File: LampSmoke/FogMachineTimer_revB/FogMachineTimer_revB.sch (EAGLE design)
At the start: 5 parts, among them IC1 ATTINY85-20SU, J1 M20-9980346, J2 CUI_PJ-037ACUI_PJ-037A_0_0, U1 LH1540AABTR

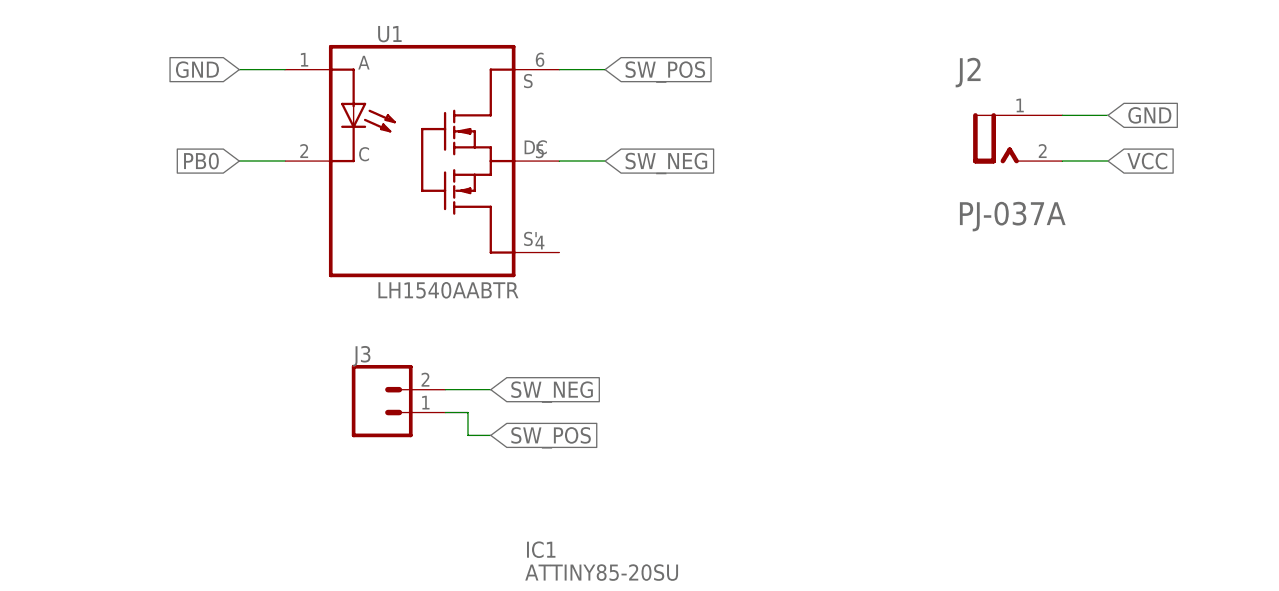
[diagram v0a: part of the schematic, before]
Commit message: corrected polarity
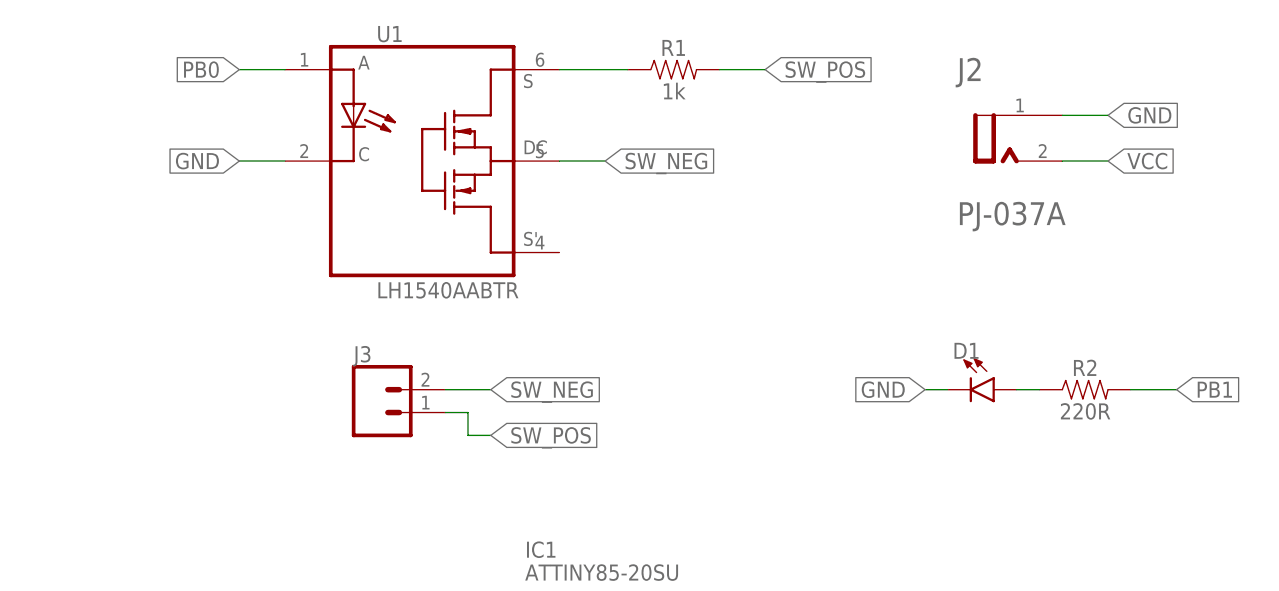
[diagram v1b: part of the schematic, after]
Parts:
- added D1: (no value), SparkFun-LED:LED1206
- added R1: 1k, SparkFun-Resistors:1KOHM-0603-1/10W-1%
- added R2: 220R, SparkFun-Resistors:1KOHM-0603-1/10W-1%
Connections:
- new net N$1: D1.A, R2.1
- new net U1_P6: R1.1, U1.S
- net GND: now also D1.C, U1.C; no longer U1.A
- net PB0: now also U1.A; no longer U1.C
- net PB1: now also R2.2
- net SW_POS: now also R1.2; no longer U1.S
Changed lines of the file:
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@@
 <part name="J2" library="NickParts" library_urn="urn:adsk.eagle:library:4753178" deviceset="CUI_PJ-037A" device="CUI_PJ-037A_0_0" package3d_urn="urn:adsk.eagle:package:4865637/3"/>
 <part name="J3" library="SparkFun-Connectors" library_urn="urn:adsk.eagle:library:513" deviceset="CONN_02" device="" package3d_urn="urn:adsk.eagle:package:38039/1"/>
+<part name="R1" library="SparkFun-Resistors" library_urn="urn:adsk.eagle:library:532" deviceset="1KOHM" device="-0603-1/10W-1%" package3d_urn="urn:adsk.eagle:package:39650/1" value="1k"/>
+<part name="D1" library="SparkFun-LED" library_urn="urn:adsk.eagle:library:529" deviceset="LED" device="1206" package3d_urn="urn:adsk.eagle:package:39352/1"/>
+<part name="R2" library="SparkFun-Resistors" library_urn="urn:adsk.eagle:library:532" deviceset="1KOHM" device="-0603-1/10W-1%" package3d_urn="urn:adsk.eagle:package:39650/1" value="220R"/>
 </parts>
 <sheets>
@@
 <attribute name="NAME" x="30.48" y="102.108" size="1.778" layer="95" font="vector"/>
 </instance>
+<instance part="R1" gate="G$1" x="66.04" y="134.62" smashed="yes">
+<attribute name="NAME" x="66.04" y="136.144" size="1.778" layer="95" font="vector" align="bottom-center"/>
+<attribute name="VALUE" x="66.04" y="133.096" size="1.778" layer="96" font="vector" align="top-center"/>
+</instance>
+<instance part="D1" gate="G$1" x="101.6" y="99.06" smashed="yes" rot="R270">
+<attribute name="NAME" x="97.028" y="102.489" size="1.778" layer="95" font="vector"/>
+<attribute name="VALUE" x="97.028" y="97.155" size="1.778" layer="96" font="vector" align="top-left"/>
+</instance>
+<instance part="R2" gate="G$1" x="111.76" y="99.06" smashed="yes">
+<attribute name="NAME" x="111.76" y="100.584" size="1.778" layer="95" font="vector" align="bottom-center"/>
+<attribute name="VALUE" x="111.76" y="97.536" size="1.778" layer="96" font="vector" align="top-center"/>
+</instance>
 </instances>
 <busses>
@@
 </segment>
 <segment>
+<pinref part="J2" gate="G$0" pin="1"/>
+<wire x1="109.22" y1="129.54" x2="114.3" y2="129.54" width="0.1524" layer="91"/>
+<label x="114.3" y="129.54" size="1.778" layer="95" xref="yes"/>
+</segment>
+<segment>
+<pinref part="U1" gate="G$1" pin="C"/>
+<wire x1="22.86" y1="124.46" x2="17.78" y2="124.46" width="0.1524" layer="91"/>
+<label x="17.78" y="124.46" size="1.778" layer="95" rot="R180" xref="yes"/>
+</segment>
+<segment>
+<pinref part="D1" gate="G$1" pin="C"/>
+<wire x1="96.52" y1="99.06" x2="93.98" y2="99.06" width="0.1524" layer="91"/>
+<label x="93.98" y="99.06" size="1.778" layer="95" rot="R180" xref="yes"/>
+</segment>
+</net>
+<net name="VCC" class="0">
+<segment>
+<pinref part="IC1" gate="G$1" pin="VCC"/>
+<wire x1="53.34" y1="66.04" x2="53.34" y2="60.96" width="0.1524" layer="91"/>
+<label x="53.34" y="60.96" size="1.778" layer="95" rot="R270" xref="yes"/>
+</segment>
+<segment>
+<pinref part="J1" gate="G$1" pin="VCC"/>
+<wire x1="22.86" y1="40.64" x2="10.16" y2="40.64" width="0.1524" layer="91"/>
+<label x="10.16" y="40.64" size="1.778" layer="95" rot="R180" xref="yes"/>
+</segment>
+<segment>
+<pinref part="J2" gate="G$0" pin="2"/>
+<wire x1="109.22" y1="124.46" x2="114.3" y2="124.46" width="0.1524" layer="91"/>
+<label x="114.3" y="124.46" size="1.778" layer="95" xref="yes"/>
+</segment>
+</net>
+<net name="PB2" class="0">
+<segment>
+<pinref part="IC1" gate="G$1" pin="SCK"/>
+<wire x1="53.34" y1="68.58" x2="58.42" y2="68.58" width="0.1524" layer="91"/>
+<label x="58.42" y="68.58" size="1.778" layer="95" xref="yes"/>
+</segment>
+<segment>
+<pinref part="J1" gate="G$1" pin="PB2/SCK/SCL"/>
+<wire x1="68.58" y1="40.64" x2="86.36" y2="40.64" width="0.1524" layer="91"/>
+<label x="86.36" y="40.64" size="1.778" layer="95" xref="yes"/>
+</segment>
+</net>
+<net name="PB1" class="0">
+<segment>
+<pinref part="IC1" gate="G$1" pin="MISO"/>
+<wire x1="53.34" y1="71.12" x2="66.04" y2="71.12" width="0.1524" layer="91"/>
+<label x="66.04" y="71.12" size="1.778" layer="95" xref="yes"/>
+</segment>
+<segment>
+<pinref part="J1" gate="G$1" pin="PB1/MISO"/>
+<wire x1="68.58" y1="43.18" x2="76.2" y2="43.18" width="0.1524" layer="91"/>
+<label x="76.2" y="43.18" size="1.778" layer="95" xref="yes"/>
+</segment>
+<segment>
+<pinref part="R2" gate="G$1" pin="2"/>
+<wire x1="116.84" y1="99.06" x2="121.92" y2="99.06" width="0.1524" layer="91"/>
+<label x="121.92" y="99.06" size="1.778" layer="95" xref="yes"/>
+</segment>
+</net>
+<net name="PB0" class="0">
+<segment>
+<pinref part="IC1" gate="G$1" pin="MOSI"/>
+<wire x1="53.34" y1="73.66" x2="58.42" y2="73.66" width="0.1524" layer="91"/>
+<label x="58.42" y="73.66" size="1.778" layer="95" xref="yes"/>
+</segment>
+<segment>
+<pinref part="J1" gate="G$1" pin="PB0/MOSI/SDA"/>
+<wire x1="22.86" y1="38.1" x2="2.54" y2="38.1" width="0.1524" layer="91"/>
+<label x="2.54" y="38.1" size="1.778" layer="95" rot="R180" xref="yes"/>
+</segment>
+<segment>
 <pinref part="U1" gate="G$1" pin="A"/>
 <wire x1="22.86" y1="134.62" x2="17.78" y2="134.62" width="0.1524" layer="91"/>
 <label x="17.78" y="134.62" size="1.778" layer="95" rot="R180" xref="yes"/>
 </segment>
-<segment>
-<pinref part="J2" gate="G$0" pin="1"/>
-<wire x1="109.22" y1="129.54" x2="114.3" y2="129.54" width="0.1524" layer="91"/>
-<label x="114.3" y="129.54" size="1.778" layer="95" xref="yes"/>
-</segment>
-</net>
-<net name="VCC" class="0">
-<segment>
-<pinref part="IC1" gate="G$1" pin="VCC"/>
-<wire x1="53.34" y1="66.04" x2="53.34" y2="60.96" width="0.1524" layer="91"/>
-<label x="53.34" y="60.96" size="1.778" layer="95" rot="R270" xref="yes"/>
-</segment>
-<segment>
-<pinref part="J1" gate="G$1" pin="VCC"/>
-<wire x1="22.86" y1="40.64" x2="10.16" y2="40.64" width="0.1524" layer="91"/>
-<label x="10.16" y="40.64" size="1.778" layer="95" rot="R180" xref="yes"/>
-</segment>
-<segment>
-<pinref part="J2" gate="G$0" pin="2"/>
-<wire x1="109.22" y1="124.46" x2="114.3" y2="124.46" width="0.1524" layer="91"/>
-<label x="114.3" y="124.46" size="1.778" layer="95" xref="yes"/>
-</segment>
-</net>
-<net name="PB2" class="0">
-<segment>
-<pinref part="IC1" gate="G$1" pin="SCK"/>
-<wire x1="53.34" y1="68.58" x2="58.42" y2="68.58" width="0.1524" layer="91"/>
-<label x="58.42" y="68.58" size="1.778" layer="95" xref="yes"/>
-</segment>
-<segment>
-<pinref part="J1" gate="G$1" pin="PB2/SCK/SCL"/>
-<wire x1="68.58" y1="40.64" x2="86.36" y2="40.64" width="0.1524" layer="91"/>
-<label x="86.36" y="40.64" size="1.778" layer="95" xref="yes"/>
-</segment>
-</net>
-<net name="PB1" class="0">
-<segment>
-<pinref part="IC1" gate="G$1" pin="MISO"/>
-<wire x1="53.34" y1="71.12" x2="66.04" y2="71.12" width="0.1524" layer="91"/>
-<label x="66.04" y="71.12" size="1.778" layer="95" xref="yes"/>
-</segment>
-<segment>
-<pinref part="J1" gate="G$1" pin="PB1/MISO"/>
-<wire x1="68.58" y1="43.18" x2="76.2" y2="43.18" width="0.1524" layer="91"/>
-<label x="76.2" y="43.18" size="1.778" layer="95" xref="yes"/>
-</segment>
-</net>
-<net name="PB0" class="0">
-<segment>
-<pinref part="IC1" gate="G$1" pin="MOSI"/>
-<wire x1="53.34" y1="73.66" x2="58.42" y2="73.66" width="0.1524" layer="91"/>
-<label x="58.42" y="73.66" size="1.778" layer="95" xref="yes"/>
-</segment>
-<segment>
-<pinref part="J1" gate="G$1" pin="PB0/MOSI/SDA"/>
-<wire x1="22.86" y1="38.1" x2="2.54" y2="38.1" width="0.1524" layer="91"/>
-<label x="2.54" y="38.1" size="1.778" layer="95" rot="R180" xref="yes"/>
-</segment>
-<segment>
-<pinref part="U1" gate="G$1" pin="C"/>
-<wire x1="22.86" y1="124.46" x2="17.78" y2="124.46" width="0.1524" layer="91"/>
-<label x="17.78" y="124.46" size="1.778" layer="95" rot="R180" xref="yes"/>
-</segment>
 </net>
 <net name="PB5" class="0">
@@
 </net>
 <net name="SW_POS" class="0">
-<segment>
-<pinref part="U1" gate="G$1" pin="S"/>
-<wire x1="53.34" y1="134.62" x2="58.42" y2="134.62" width="0.1524" layer="91"/>
-<label x="58.42" y="134.62" size="1.778" layer="95" xref="yes"/>
-</segment>
 <segment>
 <pinref part="J3" gate="G$1" pin="1"/>
@@
 <wire x1="43.18" y1="93.98" x2="45.72" y2="93.98" width="0.1524" layer="91"/>
 </segment>
-</net>
+<segment>
+<pinref part="R1" gate="G$1" pin="2"/>
+<wire x1="71.12" y1="134.62" x2="76.2" y2="134.62" width="0.1524" layer="91"/>
+<label x="76.2" y="134.62" size="1.778" layer="95" xref="yes"/>
+</segment>
+</net>
+<net name="U1_P6" class="0">
+<segment>
+<pinref part="U1" gate="G$1" pin="S"/>
+<wire x1="53.34" y1="134.62" x2="60.96" y2="134.62" width="0.1524" layer="91"/>
+<pinref part="R1" gate="G$1" pin="1"/>
+</segment>
+</net>
+<net name="N$1" class="0">
+<segment>
+<pinref part="R2" gate="G$1" pin="1"/>
+<pinref part="D1" gate="G$1" pin="A"/>
+<wire x1="106.68" y1="99.06" x2="104.14" y2="99.06" width="0.1524" layer="91"/>
+</segment>
+</net>

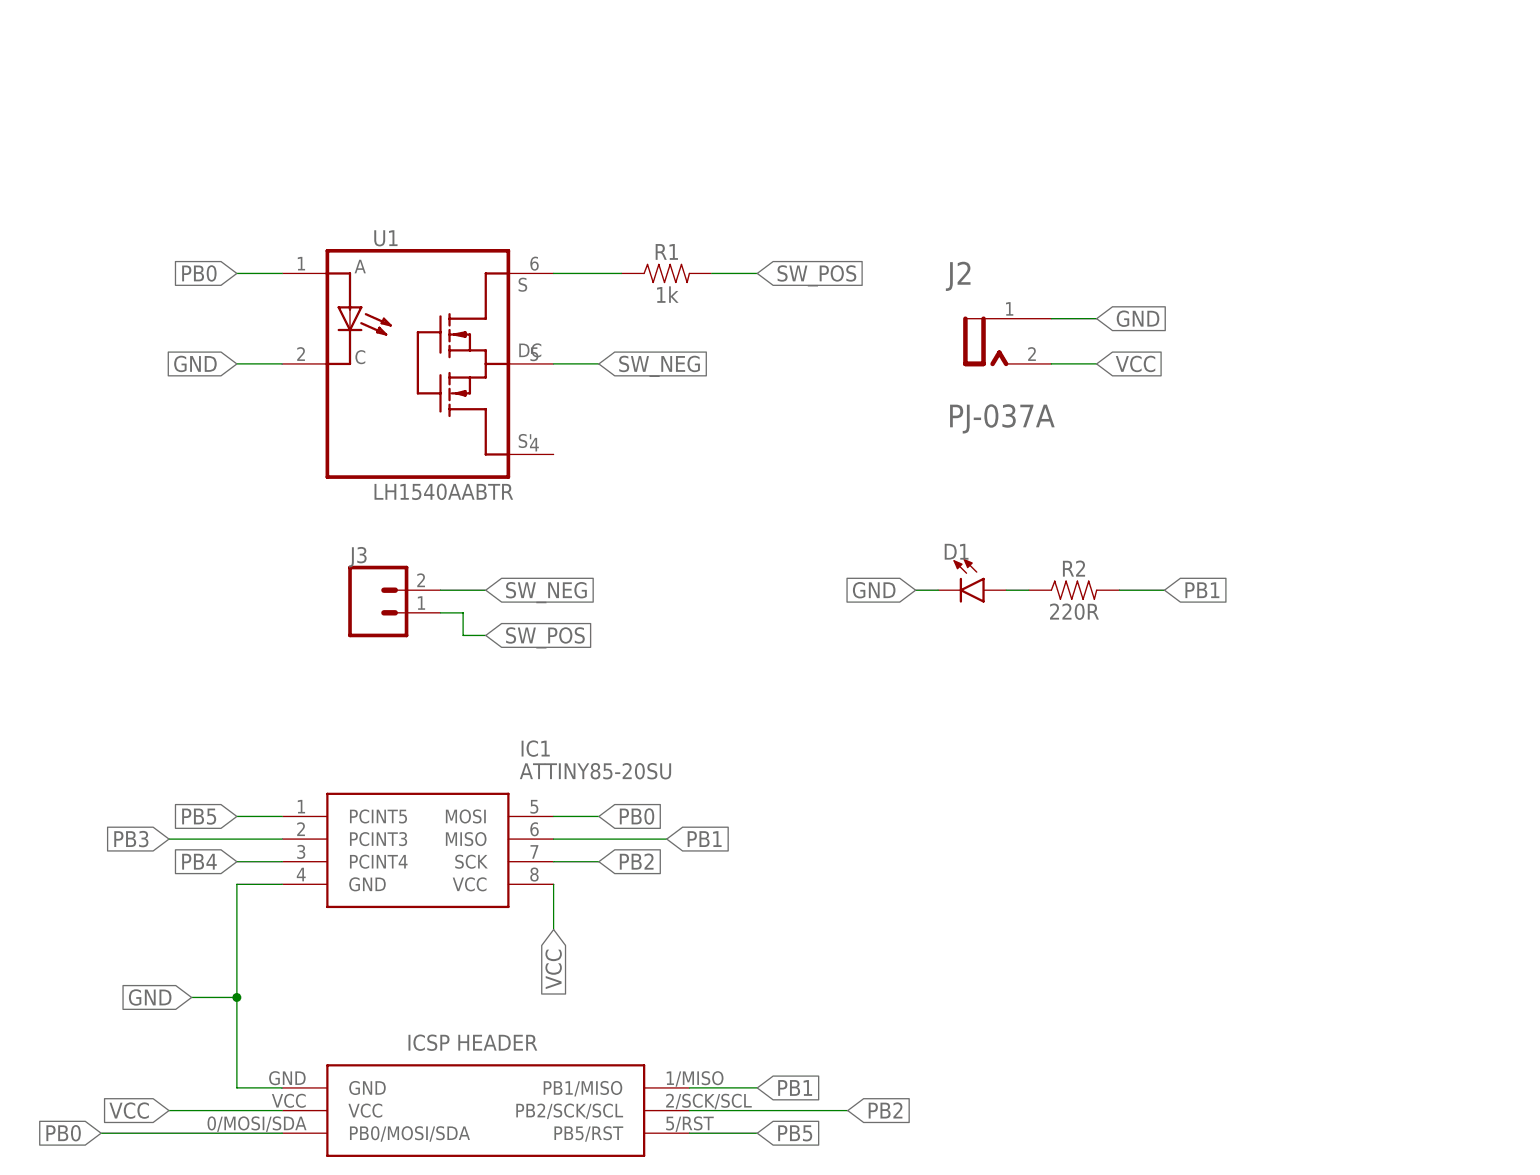
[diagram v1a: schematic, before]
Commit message: FogMachineTimer revB submitted to OSHPark
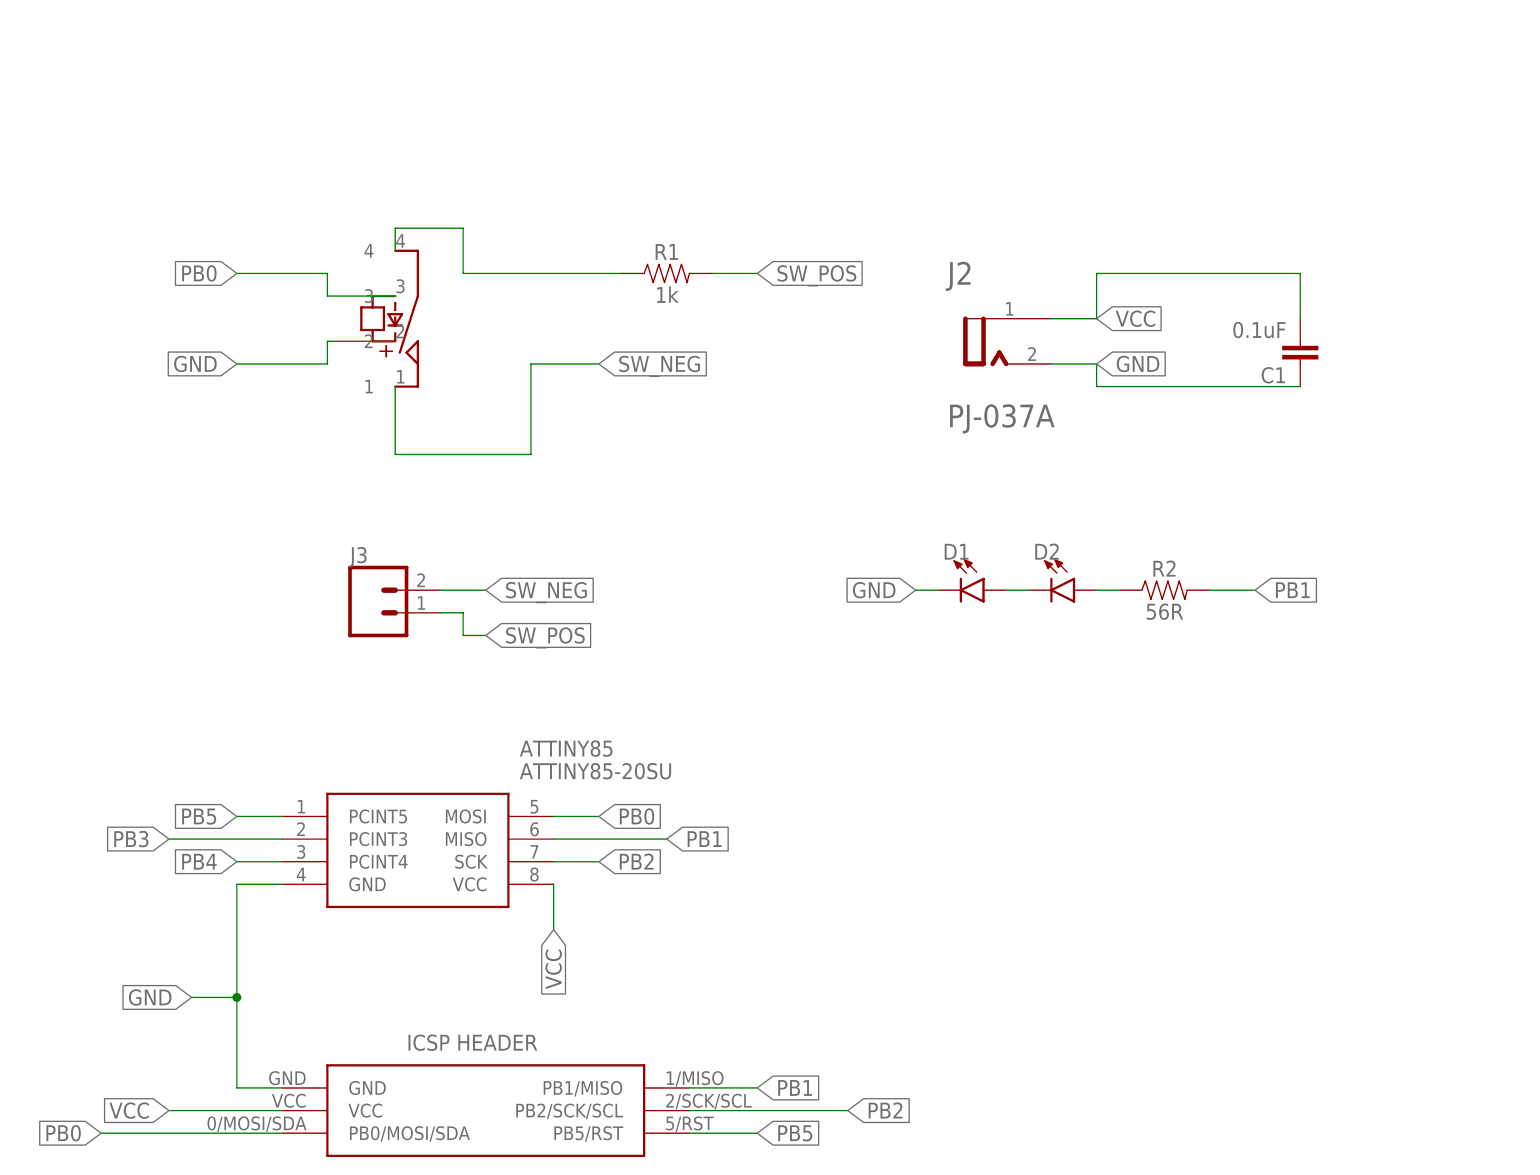
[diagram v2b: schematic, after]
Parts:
- removed U1: LH1540AABTR, NickParts:LH1540AABTR
- added C1: 0.1uF, SparkFun-Capacitors:0.1UF-0603-25V-5%
- added D2: (no value), SparkFun-LED:LED1206
- added RELAY: HE3621A0510, NickParts:HE3621A0510
- R2: value 220R -> 56R
- renumbered IC1 to ATTINY85
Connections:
- new net N$2: D2.A, R2.1
- net GND: now also C1.1, J2.2, RELAY.2; no longer J2.1, U1.C
- net N$1: now also D2.C; no longer R2.1
- net PB0: now also RELAY.3; no longer U1.A
- net SW_NEG: now also RELAY.1; no longer U1.DC
- net U1_P6: now also RELAY.4; no longer U1.S
- net VCC: now also C1.2, J2.1; no longer J2.2
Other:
- moved on the sheet: R2
